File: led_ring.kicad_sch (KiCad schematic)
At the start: 24 parts

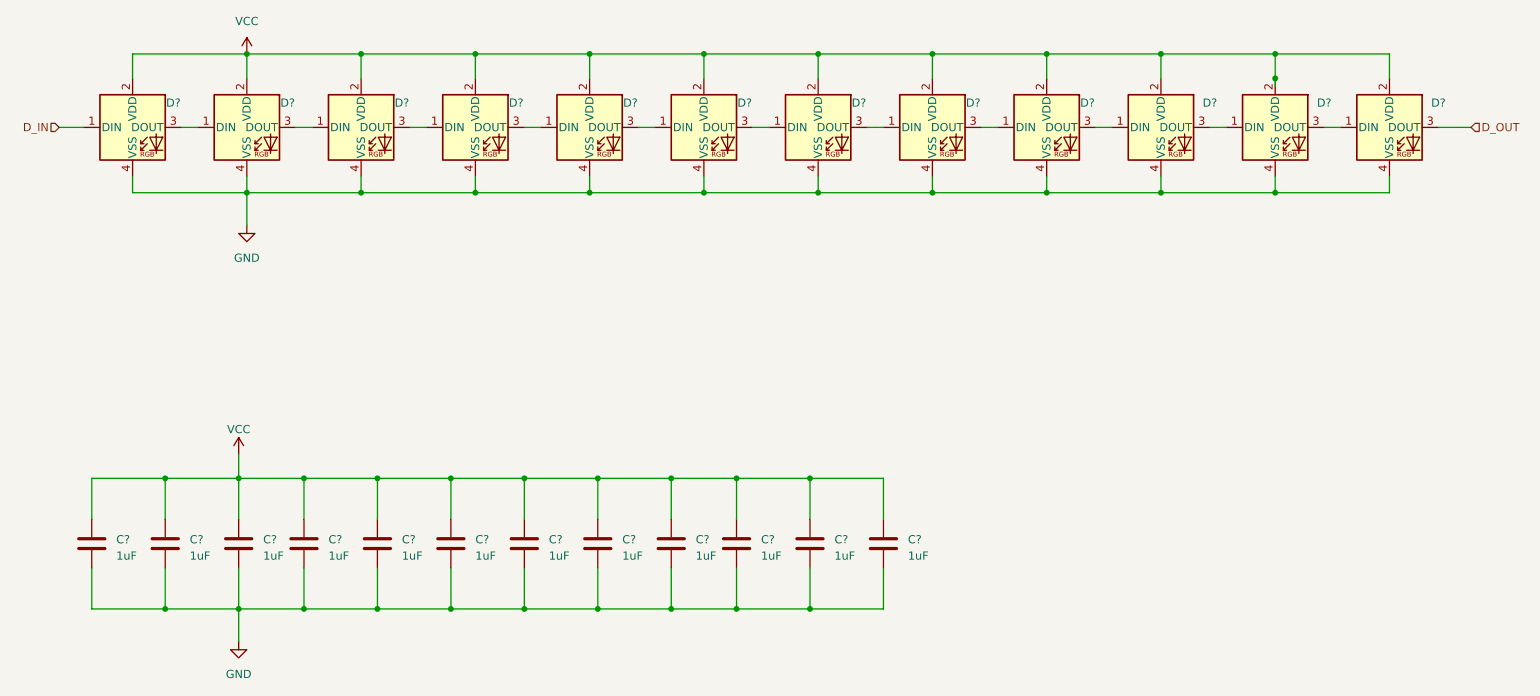
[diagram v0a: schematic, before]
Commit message: Connectedx all LEDs
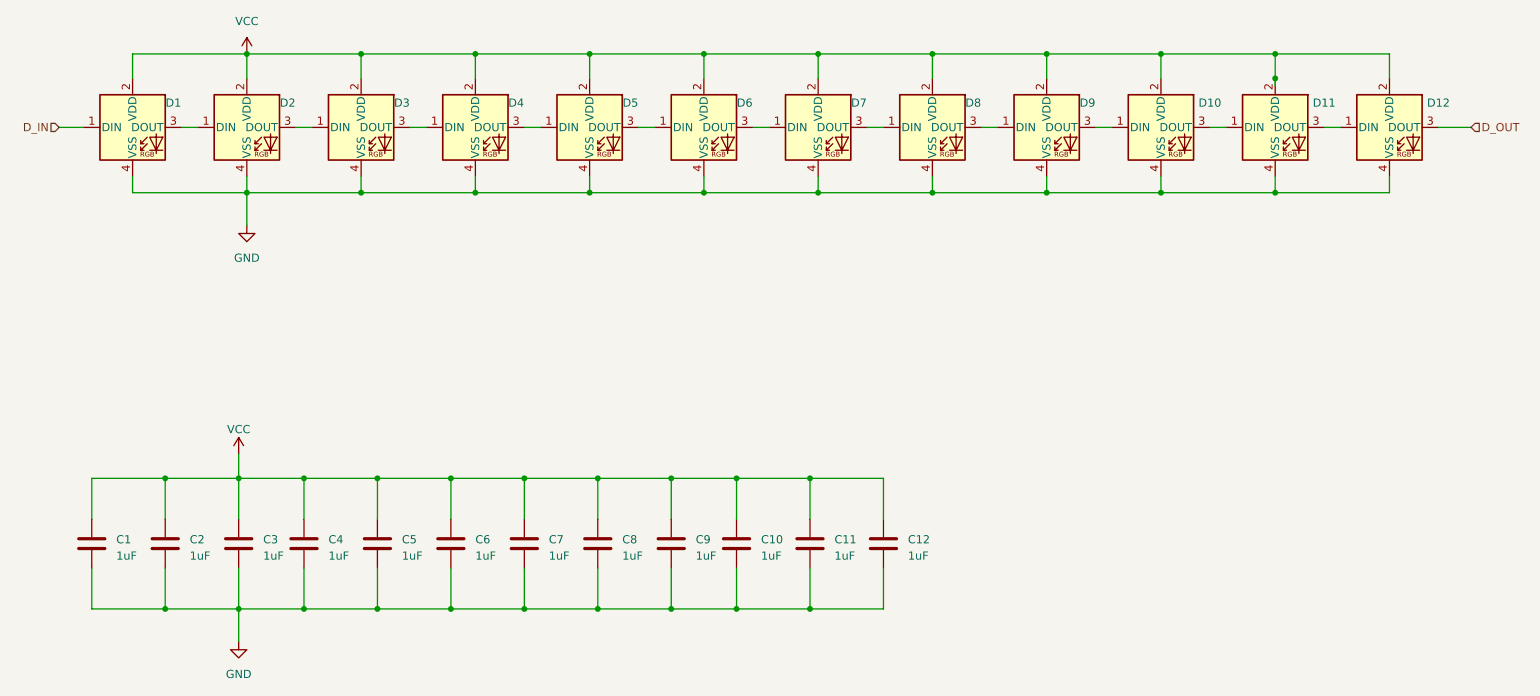
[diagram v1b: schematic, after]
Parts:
- gave numbers to parts that had none: 24
